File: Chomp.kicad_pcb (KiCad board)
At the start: 2 copper layers, 95.2 x 41.3 mm, 34 parts, among them J1 IN2, J10 V1-6, J11 V1-8, J12 V2-5, J13 V2-8, J14 V2-4, J15 T1-4, J16 T1-2, J2 IN1, J3 V1-2, J4 V1-1, J5 V1-3, J6 RV1-1, J7 RV1-3, J8 RV1-2, J9 V1-7

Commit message: Fix edge cut
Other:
- board size 95.2 x 41.3 mm -> 95.2 x 44.5 mm
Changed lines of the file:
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@@
     )
   )
-  (gr_rect (start 174.625 68.2625) (end 79.375 109.5375) (layer "Edge.Cuts") (width 0.1) (fill none))
+  (gr_rect (start 174.625 82.55) (end 79.375 127) (layer "Edge.Cuts") (width 0.1) (fill none))
   (gr_text "10" (at 139.7 82.325) (layer "Cmts.User")
     (effects (font (size 1 1) (thickness 0.15)))

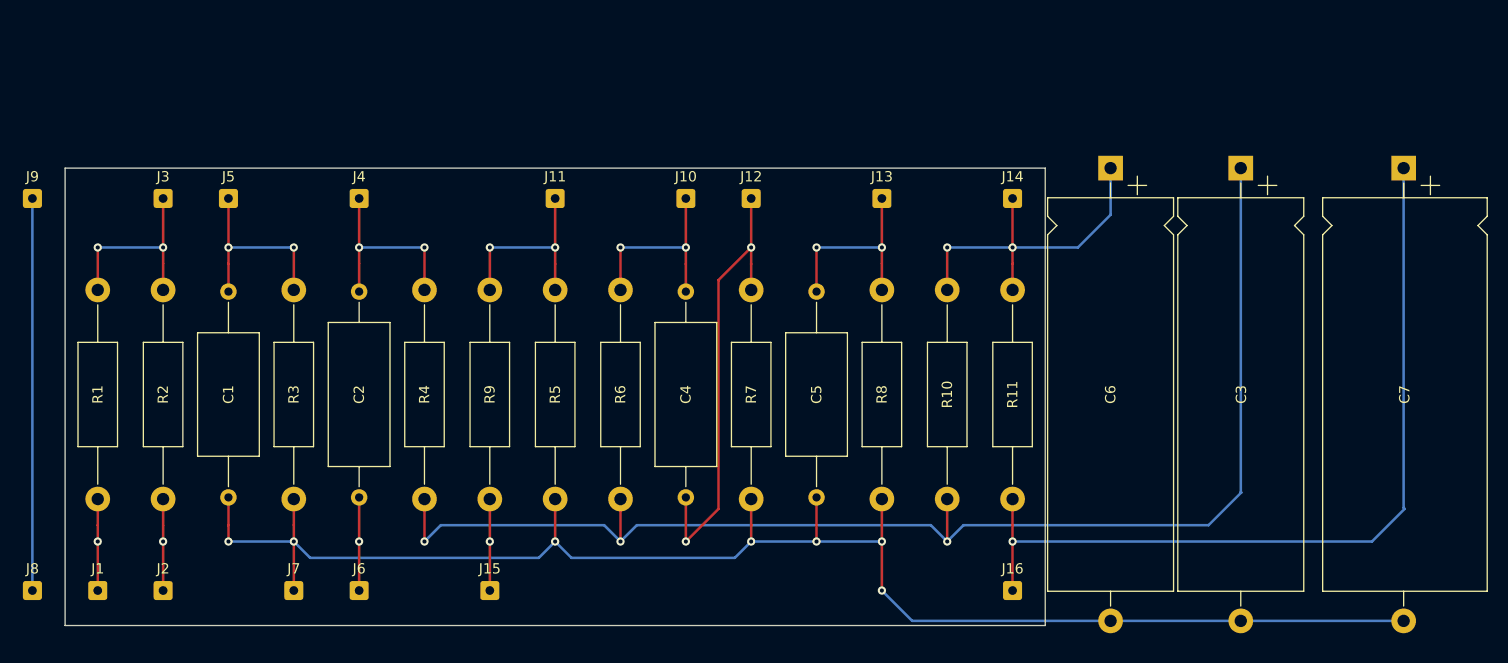
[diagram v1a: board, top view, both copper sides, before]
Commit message: Ground routing and layout tweaks.
http://www.valvewizard.co.uk/Grounding.pdf gives some good advice on grounding using a Champ circuit as an example. Rather than leave the schematic ambigous on this topic, I've drawn Blencowe's recommendations directly. The layout matches the schematic almost exactly, though the ordering of the elecrolytic grounds is constrained by reality, and the output ground is tied where convenient.
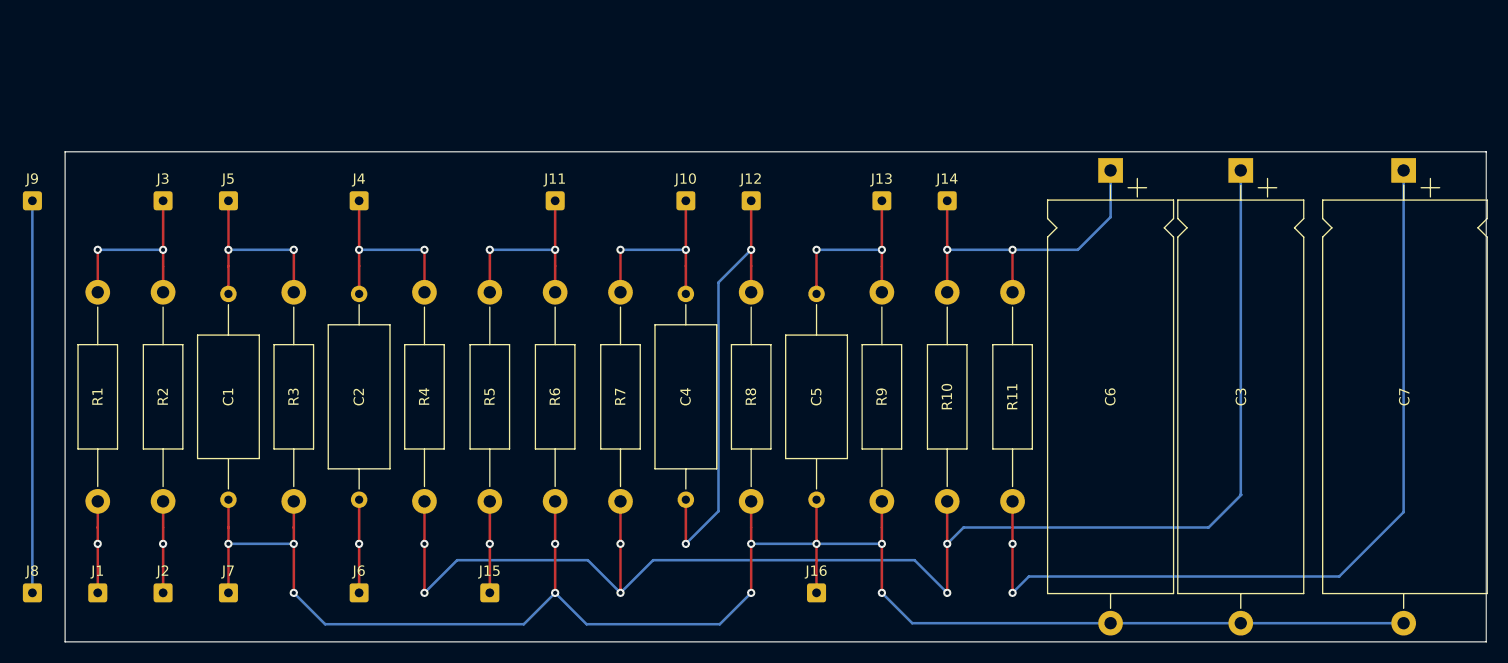
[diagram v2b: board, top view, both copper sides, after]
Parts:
- J15: value T1-4 -> T2-G
- J16: value T1-2 -> T2-B
- moved J16 19.1 mm to (152.4, 123.8)
- moved J14 6.35 mm to (165.1, 85.7)
- moved J7 6.35 mm to (95.2, 123.8)
- moved C1 0.23 mm to (95.2, 94.8)
- moved C2 0.23 mm to (108.0, 94.8)
- moved C3 0.23 mm to (193.6, 82.8)
- moved C4 0.23 mm to (139.7, 94.8)
- moved C5 0.23 mm to (152.4, 94.8)
- moved C6 0.23 mm to (181.0, 82.8)
- moved C7 0.23 mm to (209.5, 82.8)
- moved J1 0.23 mm to (82.5, 123.8)
- moved J15 0.23 mm to (120.7, 123.8)
- moved J2 0.23 mm to (88.9, 123.8)
- moved J6 0.23 mm to (108.0, 123.8)
- moved J8 0.23 mm to (76.2, 123.8)
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- renumbered R9 to R5, R5 to R6, R6 to R7, R7 to R8, R8 to R9
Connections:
- C1 pad 2: GND -> GNDPWR
- C3 pad 2: GND -> GNDPWR
- C5 pad 2: GND -> GNDPWR
- C6 pad 2: GND -> GNDPWR
- C7 pad 2: GND -> GNDPWR
- J16 pad 1: Net-(C7-Pad1) -> GNDPWR
- J7 pad 1: GND -> GNDPWR
- R3 pad 2: GND -> GNDPWR
- R6 pad 2: GND -> GNDPWR
- R8 pad 2: GND -> GNDPWR
- R9 pad 2: GND -> GNDPWR
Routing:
- net GNDPWR: track 0.00 -> 174.1 mm, vias 0 -> 10
- net GND: track 152.7 -> 0.00 mm, vias 7 -> 0
- net Net-(C3-Pad1): track 127.9 -> 144.8 mm, vias 3 -> 6
- net Net-(C7-Pad1): track 81.5 -> 83.4 mm, vias 1 -> 2
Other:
- board size 95.2 x 44.5 mm -> 138.1 x 47.6 mm

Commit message: Update the layout diagram to reflect the final build.
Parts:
- moved J3 6.35 mm to (82.5, 85.7)
- moved J10 6.35 mm to (133.3, 85.7)
- moved J11 6.35 mm to (120.7, 85.7)
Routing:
- net Net-(C3-Pad1): track 144.8 -> 146.8 mm
- net Net-(C6-Pad1): track 34.7 -> 34.9 mm, vias 2 -> 3
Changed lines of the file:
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@@
   )
   (footprint "Connector_Wire:SolderWire-0.25sqmm_1x01_D0.65mm_OD1.7mm" (layer "F.Cu")
-    (at 127 85.725)
+    (at 120.65 85.725)
     (descr "Soldered wire connection, for a single 0.25 mm² wire, basic insulation, conductor diameter 0.65mm, outer diameter 1.7mm, size source Multi-Contact FLEXI-E_0.25 (https://ec.staubli.com/AcroFiles/Catalogues/TM_Cab-Main-11014119_(en)_hi.pdf), bend radius 3 times outer diameter, generated with kicad-footprint-generator")
     (tags "connector wire 0.25sqmm")
@@
   )
   (footprint "Connector_Wire:SolderWire-0.25sqmm_1x01_D0.65mm_OD1.7mm" (layer "F.Cu")
-    (at 88.9 85.725)
+    (at 82.55 85.725)
     (descr "Soldered wire connection, for a single 0.25 mm² wire, basic insulation, conductor diameter 0.65mm, outer diameter 1.7mm, size source Multi-Contact FLEXI-E_0.25 (https://ec.staubli.com/AcroFiles/Catalogues/TM_Cab-Main-11014119_(en)_hi.pdf), bend radius 3 times outer diameter, generated with kicad-footprint-generator")
     (tags "connector wire 0.25sqmm")
@@
   )
   (footprint "Connector_Wire:SolderWire-0.25sqmm_1x01_D0.65mm_OD1.7mm" (layer "F.Cu")
-    (at 139.7 85.725)
+    (at 133.35 85.725)
     (descr "Soldered wire connection, for a single 0.25 mm² wire, basic insulation, conductor diameter 0.65mm, outer diameter 1.7mm, size source Multi-Contact FLEXI-E_0.25 (https://ec.staubli.com/AcroFiles/Catalogues/TM_Cab-Main-11014119_(en)_hi.pdf), bend radius 3 times outer diameter, generated with kicad-footprint-generator")
     (tags "connector wire 0.25sqmm")
@@
   (via (at 88.9 119.0625) (size 0.8) (drill 0.4) (layers "F.Cu" "B.Cu") (net 3))
   (segment (start 82.55 94.615) (end 82.55 90.4875) (width 0.25) (layer "F.Cu") (net 4))
-  (segment (start 88.9 94.615) (end 88.9 92.075) (width 0.25) (layer "F.Cu") (net 4))
-  (segment (start 88.9 92.075) (end 88.9 85.725) (width 0.25) (layer "F.Cu") (net 4))
+  (segment (start 82.55 85.725) (end 82.55 90.4875) (width 0.25) (layer "F.Cu") (net 4))
+  (segment (start 88.9 94.615) (end 88.9 90.4875) (width 0.25) (layer "F.Cu") (net 4))
   (via (at 82.55 90.4875) (size 0.8) (drill 0.4) (layers "F.Cu" "B.Cu") (free) (net 4))
   (via (at 88.9 90.4875) (size 0.8) (drill 0.4) (layers "F.Cu" "B.Cu") (net 4))
@@
   (via (at 107.95 119.0625) (size 0.8) (drill 0.4) (layers "F.Cu" "B.Cu") (net 7))
   (segment (start 139.54 94.615) (end 139.7 94.775) (width 0.25) (layer "F.Cu") (net 8))
-  (segment (start 139.7 94.775) (end 139.7 92.075) (width 0.25) (layer "F.Cu") (net 8))
+  (segment (start 133.35 90.4875) (end 133.35 85.725) (width 0.25) (layer "F.Cu") (net 8))
+  (segment (start 139.7 94.775) (end 139.7 90.4875) (width 0.25) (layer "F.Cu") (net 8))
   (segment (start 133.35 94.615) (end 133.35 90.4875) (width 0.25) (layer "F.Cu") (net 8))
-  (segment (start 139.7 92.075) (end 139.7 85.725) (width 0.25) (layer "F.Cu") (net 8))
   (via (at 139.7 90.4875) (size 0.8) (drill 0.4) (layers "F.Cu" "B.Cu") (net 8))
   (via (at 133.35 90.4875) (size 0.8) (drill 0.4) (layers "F.Cu" "B.Cu") (free) (net 8))
@@
   (via (at 133.35 123.825) (size 0.8) (drill 0.4) (layers "F.Cu" "B.Cu") (net 12))
   (via (at 165.1 119.0625) (size 0.8) (drill 0.4) (layers "F.Cu" "B.Cu") (net 12))
-  (segment (start 190.5 117.475) (end 193.675 114.3) (width 0.25) (layer "B.Cu") (net 12))
+  (segment (start 193.6275 114.3475) (end 193.6275 114.2525) (width 0.25) (layer "B.Cu") (net 12))
   (segment (start 114.3 123.825) (end 117.475 120.65) (width 0.25) (layer "B.Cu") (net 12))
-  (segment (start 166.6875 117.475) (end 190.5 117.475) (width 0.25) (layer "B.Cu") (net 12))
   (segment (start 117.475 120.65) (end 130.175 120.65) (width 0.25) (layer "B.Cu") (net 12))
   (segment (start 133.35 123.825) (end 136.525 120.65) (width 0.25) (layer "B.Cu") (net 12))
   (segment (start 136.525 120.65) (end 161.925 120.65) (width 0.25) (layer "B.Cu") (net 12))
   (segment (start 193.6275 114.2525) (end 193.6275 82.775) (width 0.25) (layer "B.Cu") (net 12))
+  (segment (start 187.325 120.65) (end 193.6275 114.3475) (width 0.25) (layer "B.Cu") (net 12))
+  (segment (start 168.275 120.65) (end 187.325 120.65) (width 0.25) (layer "B.Cu") (net 12))
   (segment (start 193.675 114.3) (end 193.6275 114.2525) (width 0.25) (layer "B.Cu") (net 12))
-  (segment (start 165.1 119.0625) (end 166.6875 117.475) (width 0.25) (layer "B.Cu") (net 12))
   (segment (start 130.175 120.65) (end 133.35 123.825) (width 0.25) (layer "B.Cu") (net 12))
   (segment (start 161.925 120.65) (end 165.1 123.825) (width 0.25) (layer "B.Cu") (net 12))
+  (segment (start 165.1 123.825) (end 168.275 120.65) (width 0.25) (layer "B.Cu") (net 12))
   (segment (start 165.1 90.4875) (end 165.1 85.725) (width 0.25) (layer "F.Cu") (net 13))
   (segment (start 171.45 94.615) (end 171.45 90.4875) (width 0.25) (layer "F.Cu") (net 13))
+  (segment (start 171.45 90.4875) (end 171.45 85.725) (width 0.25) (layer "F.Cu") (net 13))
   (segment (start 165.1 94.615) (end 165.1 90.4875) (width 0.25) (layer "F.Cu") (net 13))
   (via (at 171.45 90.4875) (size 0.8) (drill 0.4) (layers "F.Cu" "B.Cu") (net 13))
   (via (at 165.1 90.4875) (size 0.8) (drill 0.4) (layers "F.Cu" "B.Cu") (free) (net 13))
-  (segment (start 171.45 90.4875) (end 177.8 90.4875) (width 0.25) (layer "B.Cu") (net 13))
-  (segment (start 180.975 87.3125) (end 180.975 82.775) (width 0.25) (layer "B.Cu") (net 13))
+  (via (at 171.45 85.725) (size 0.8) (drill 0.4) (layers "F.Cu" "B.Cu") (net 13))
   (segment (start 171.45 90.4875) (end 165.1 90.4875) (width 0.25) (layer "B.Cu") (net 13))
-  (segment (start 177.8 90.4875) (end 180.975 87.3125) (width 0.25) (layer "B.Cu") (net 13))
+  (segment (start 171.45 85.725) (end 178.025 85.725) (width 0.25) (layer "B.Cu") (net 13))
+  (segment (start 178.025 85.725) (end 180.975 82.775) (width 0.25) (layer "B.Cu") (net 13))
   (segment (start 76.2 123.825) (end 76.2 85.725) (width 0.25) (layer "B.Cu") (net 14))
-  (segment (start 127 94.615) (end 127 92.075) (width 0.25) (layer "F.Cu") (net 15))
-  (segment (start 127 92.075) (end 127 85.725) (width 0.25) (layer "F.Cu") (net 15))
+  (segment (start 127 94.615) (end 127 90.4875) (width 0.25) (layer "F.Cu") (net 15))
+  (segment (start 120.65 90.4875) (end 120.65 85.725) (width 0.25) (layer "F.Cu") (net 15))
   (segment (start 120.65 94.615) (end 120.65 90.4875) (width 0.25) (layer "F.Cu") (net 15))
   (via (at 127 90.4875) (size 0.8) (drill 0.4) (layers "F.Cu" "B.Cu") (net 15))

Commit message: Improve labeling.
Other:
- board text added: "B+1"
- board text added: "B+2"
- board text added: "B+3"
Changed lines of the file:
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@@
     (effects (font (size 1 1) (thickness 0.15)))
+  )
+  (gr_text "B+2" (at 180.975 79.375) (layer "Cmts.User")
+    (effects (font (size 1.5 1.5) (thickness 0.15)))
   )
   (gr_text "14" (at 165.1 82.55) (layer "Cmts.User")
@@
     (effects (font (size 1 1) (thickness 0.15)))
   )
+  (gr_text "B+3" (at 193.675 79.375) (layer "Cmts.User")
+    (effects (font (size 1.5 1.5) (thickness 0.15)))
+  )
   (gr_text "5" (at 107.95 82.55) (layer "Cmts.User")
     (effects (font (size 1 1) (thickness 0.15)))
@@
     (effects (font (size 1 1) (thickness 0.15)))
   )
+  (gr_text "B+1" (at 209.55 79.375) (layer "Cmts.User")
+    (effects (font (size 1.5 1.5) (thickness 0.15)))
+  )
   (gr_text "Rivet holes -" (at 69.85 119.0625) (layer "Cmts.User")

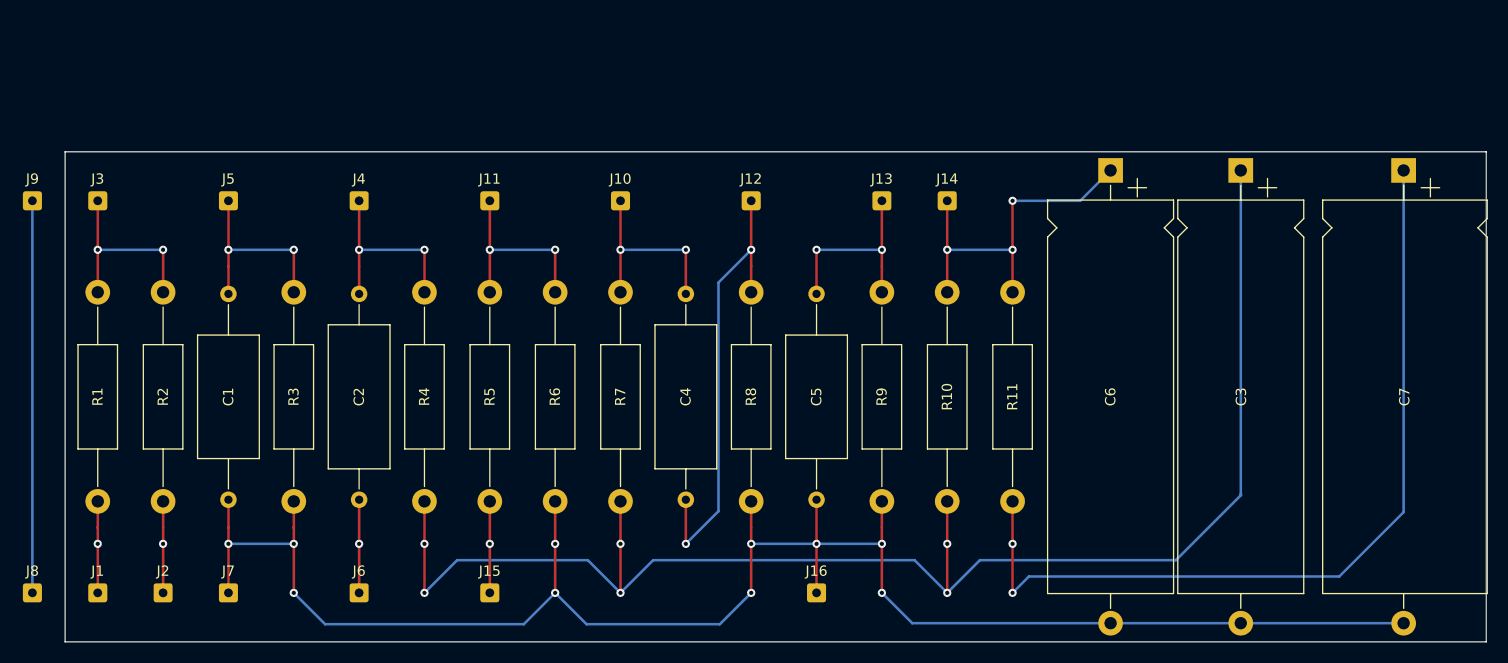
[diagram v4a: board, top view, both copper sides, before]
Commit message: Restructure the schematic layout to emphasize power.
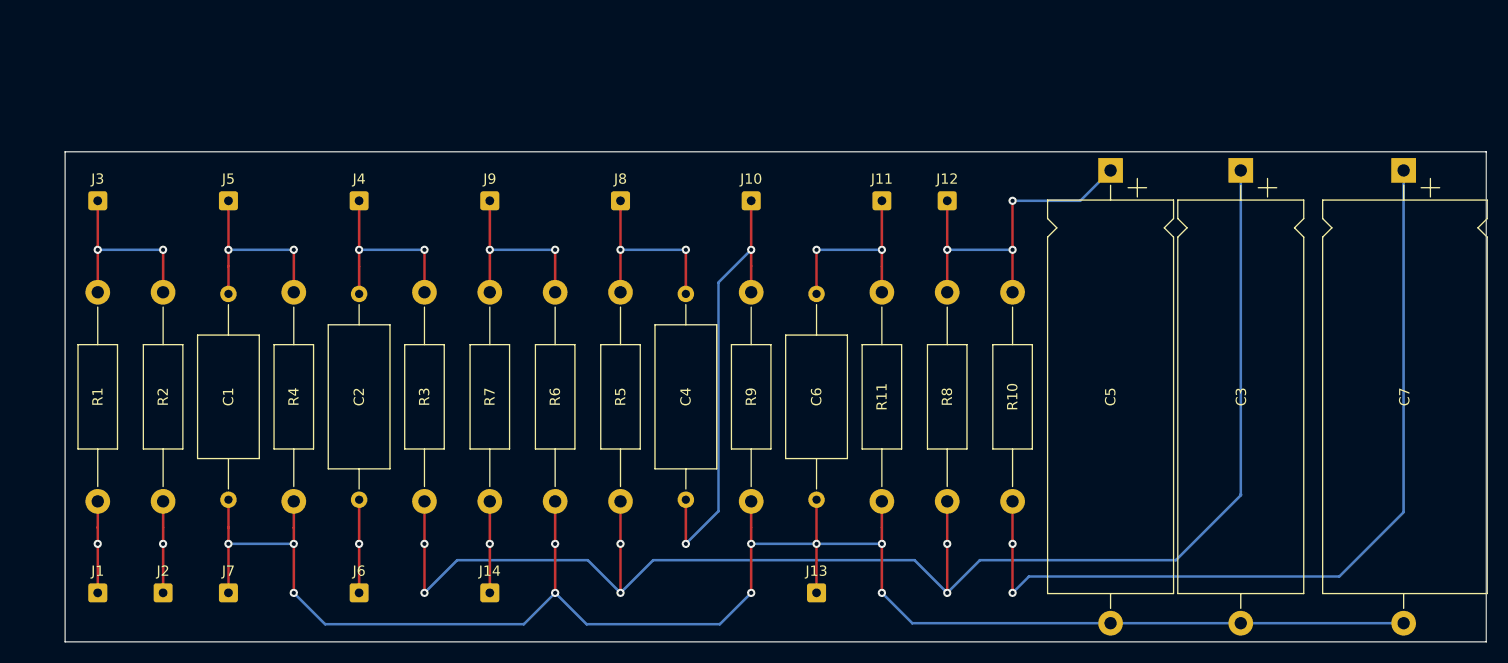
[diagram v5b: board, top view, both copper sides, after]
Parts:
- removed the J8 at (76.2, 123.8)
- removed the J9 at (76.2, 85.7)
- moved R3 20.3 mm to (114.3, 114.9), turned to 90 degrees
- moved R5 20.3 mm to (133.3, 114.9), turned to 90 degrees
- renumbered C6 to C5, C5 to C6, J12 to J10, J13 to J11, J14 to J12, J16 to J13, J15 to J14, J10 to J8, J11 to J9, R11 to R10, R9 to R11, R4 to R3, R3 to R4, R7 to R5, R5 to R7, R10 to R8, R8 to R9
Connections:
- net GNDPWR renamed GND
- R3 pad 1: Net-(C2-Pad1) -> Net-(C3-Pad1)
- R3 pad 2: Net-(C3-Pad1) -> Net-(C2-Pad1)
- R5 pad 1: Net-(C4-Pad1) -> Net-(C3-Pad1)
- R5 pad 2: Net-(C3-Pad1) -> Net-(C4-Pad1)
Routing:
- net Net-(J8-Pad1): track 38.1 -> 0.00 mm

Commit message: Reorient OT and add screen resistor.
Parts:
- J12: value V2-4 -> V2-6
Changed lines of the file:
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@@
       (effects (font (size 1 1) (thickness 0.15)))
     )
-    (fp_text value "V2-4" (at 0 2.12) (layer "F.Fab")
+    (fp_text value "V2-6" (at 0 2.12) (layer "F.Fab")
       (effects (font (size 1 1) (thickness 0.15)))
     )
